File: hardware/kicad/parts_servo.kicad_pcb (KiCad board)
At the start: 2 copper layers, 37.3 x 17.5 mm, 47 parts, among them Q110 NFET-DUAL, Q120 NFET-DUAL, U1 MCP1703-3302, U100 RT9625A, U200 AS5050, U50 NRF51822, X60 16MHz

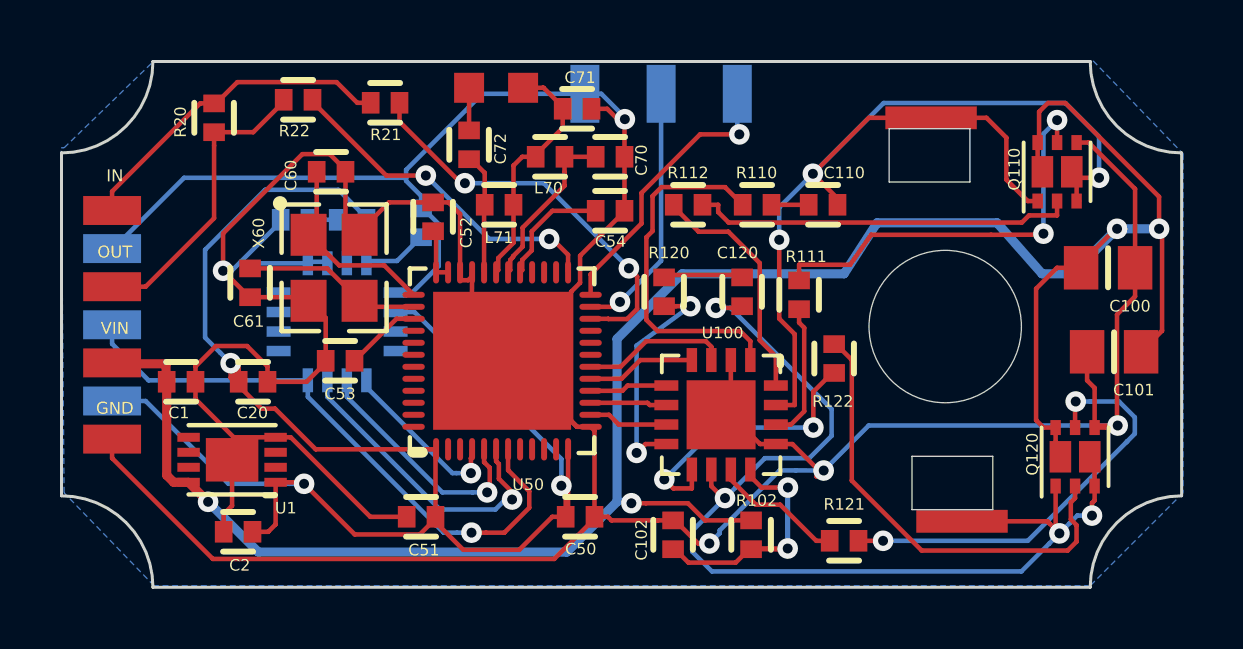
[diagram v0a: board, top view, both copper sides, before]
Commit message: Fix incorrect connections on AS5050
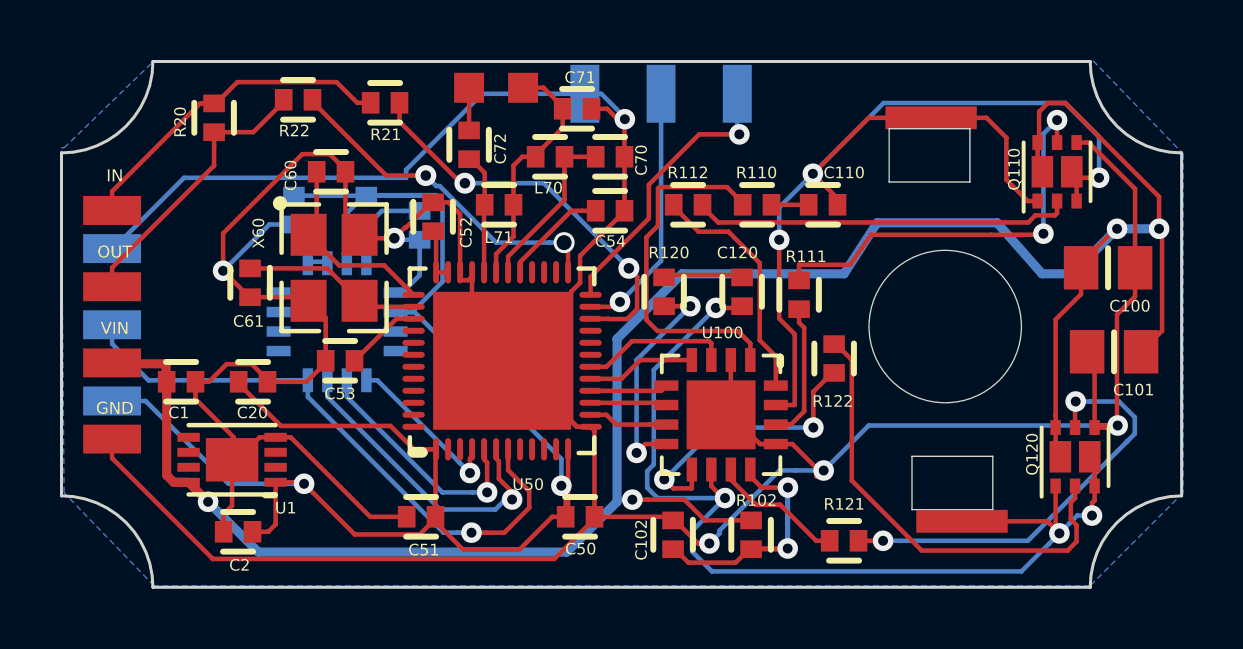
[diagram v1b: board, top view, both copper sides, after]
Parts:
- moved C203 4.26 mm to (137.5, 101.2), turned to 270 degrees
- moved C204 4.16 mm to (141.7, 101.7), turned to 90 degrees
- moved R201 0.57 mm to (140.0, 101.2), turned to 90 degrees
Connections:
- net /VIN renamed Net-(C1-Pad1)
- C2 pad 1: VDD -> +3.3V
- C20 pad 1: VDD -> +3.3V
- C203 pad 1: VDD -> +3.3V
- C50 pad 1: VDD -> +3.3V
- C51 pad 1: VDD -> +3.3V
- JP5 pad 3: VDD -> +3.3V
- R201 pad 2: VDD -> +3.3V
- U1 pad 1: VDD -> +3.3V
- U200 pad 11: Net-(C204-Pad2) -> +3.3V
- U200 pad 12: VDD -> Net-(C204-Pad2)
- U200 pad 14: VDD -> +3.3V
- U50 pad 1: VDD -> +3.3V
- U50 pad 12: VDD -> +3.3V
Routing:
- net VDD: track 60.2 -> 0.00 mm, vias 3 -> 0
- net +3.3V: track 0.00 -> 58.5 mm, vias 0 -> 2
- net GND: track 152.9 -> 150.7 mm, vias 5 -> 6
- net Net-(C1-Pad1): track 76.6 -> 75.4 mm
- net Net-(C120-Pad2): track 36.3 -> 35.5 mm
- net Net-(JP2-Pad3): track 10.0 -> 9.36 mm
- net Net-(C204-Pad2): track 2.80 -> 3.39 mm
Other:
- net class Default: via_dia 0.889 -> 0.7; via_drill 0.635 -> 0.5

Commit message: New board layout.  Version sent to DirtyPCBs for thinner boards
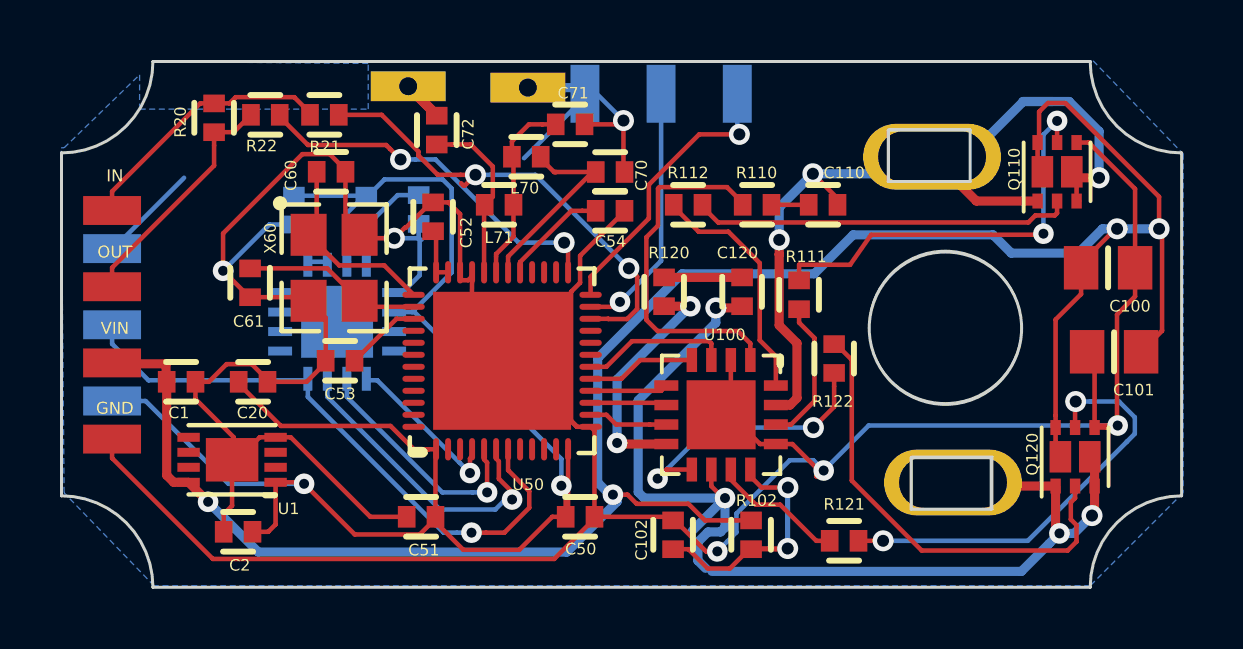
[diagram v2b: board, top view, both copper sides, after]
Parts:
- U200: footprint parts_servo:AS5550 -> parts_servo:AS5050
- moved R21 2.06 mm to (138.6, 98.0)
- moved TP2 2.03 mm to (141.4, 97.1), turned to 0 degrees
- moved JP1 1.33 mm to (159.5, 110.3)
- moved JP3 1.30 mm to (158.8, 99.4)
- moved R22 1.20 mm to (136.6, 98.0)
- moved C72 1.18 mm to (142.3, 98.6)
- moved TP1 0.90 mm to (146.0, 97.5), turned to 180 degrees
- moved L70 0.79 mm to (145.3, 99.4)
- moved C71 0.57 mm to (146.7, 98.4)
- moved C204 0.53 mm to (141.7, 101.2)
- moved C70 0.51 mm to (148.1, 99.9)
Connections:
- net Net-(C1-Pad1) renamed /PWR_IN
- net Net-(C110-Pad2) renamed /PWR_MotorB
- net Net-(C120-Pad2) renamed /PWR_MotorA
- TP1 pad TP: Net-(C71-Pad1) -> GND
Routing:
- net GND: track 150.7 -> 141.0 mm
- net /PWR_MotorA: track 35.5 -> 39.1 mm
- net /PWR_MotorB: track 36.4 -> 33.6 mm
- net Net-(C72-Pad2): track 1.42 -> 4.10 mm
- net /UNIPOLAR_INPUT: track 13.5 -> 15.7 mm
- net Net-(JP2-Pad4): track 11.0 -> 8.88 mm
- net Net-(C71-Pad1): track 8.54 -> 6.48 mm
- net Net-(C72-Pad1): track 4.03 -> 5.82 mm
- net +3.3V: track 58.5 -> 56.8 mm
- net Net-(JP2-Pad3): track 9.36 -> 8.03 mm
- net Net-(C70-Pad1): track 5.67 -> 6.83 mm
- net /UNIPOLAR_OUTPUT: track 11.4 -> 12.3 mm
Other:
- outline, holes or cut-outs redrawn
- net class PWR added: clearance 0.1524, trace_width 0.3048, via_dia 0.7, via_drill 0.5

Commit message: board layout cleanup
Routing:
- net Net-(C102-Pad1): track 11.3 -> 8.03 mm
- net /PWR_MotorA: track 39.1 -> 36.2 mm
- net GND: track 141.0 -> 143.5 mm
- net /PWR_MotorB: track 33.6 -> 32.5 mm
- net /UNIPOLAR_INPUT: track 15.7 -> 15.0 mm
